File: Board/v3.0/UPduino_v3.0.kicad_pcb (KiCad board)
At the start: 4 copper layers, 62 x 22.2 mm, 114 parts, among them J1 47589-0001, J2 Right, J3 Left, J4 5V Power, U1 93LC56BT-I/OT, U2 ICE40UP5K-SG48ITR, U3 FT232H, U4 SG-210STF 12.0000ML3, U5 W25Q32JVSSIM, U6 AP2127K-3.3, U7 AP2127K-1.2, U8 SN74AUP2G125DCUR

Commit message: Removed CE logo, added RoHS logo, regenerated gerbers.
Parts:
- removed the REF** at (125.6, 92.5)
- added REF**: RoHS-Logo_3mm_SilkScreen, Symbol:RoHS-Logo_3mm_SilkScreen - Copy, B.Cu at (134.3, 94.9)

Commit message: Updated gerbers and fab files
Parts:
- moved D3 0.25 mm to (110.9, 87.0)
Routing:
- net /LED_B: track 42.5 -> 44.2 mm
- net /IOT_51A: track 15.4 -> 14.5 mm

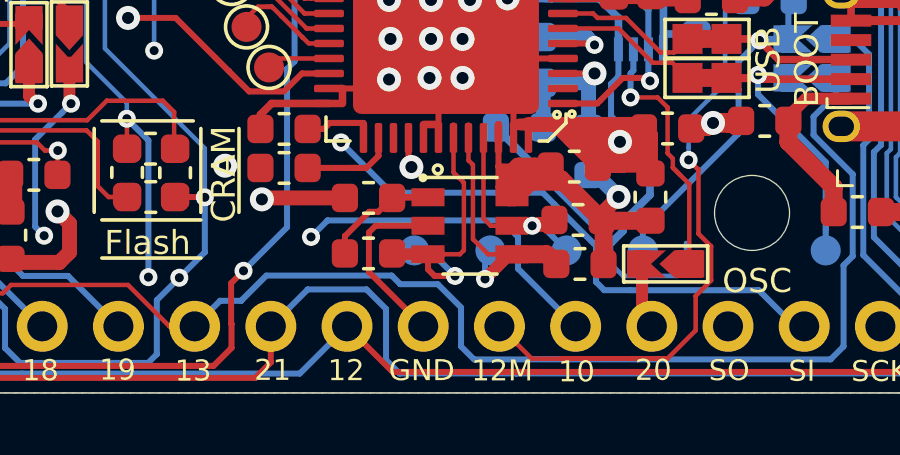
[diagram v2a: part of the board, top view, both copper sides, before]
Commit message: Bugfix for 12MHz clock pin
@ggrummer identified a bug that the 12MHz clock and ground pins are swapped.
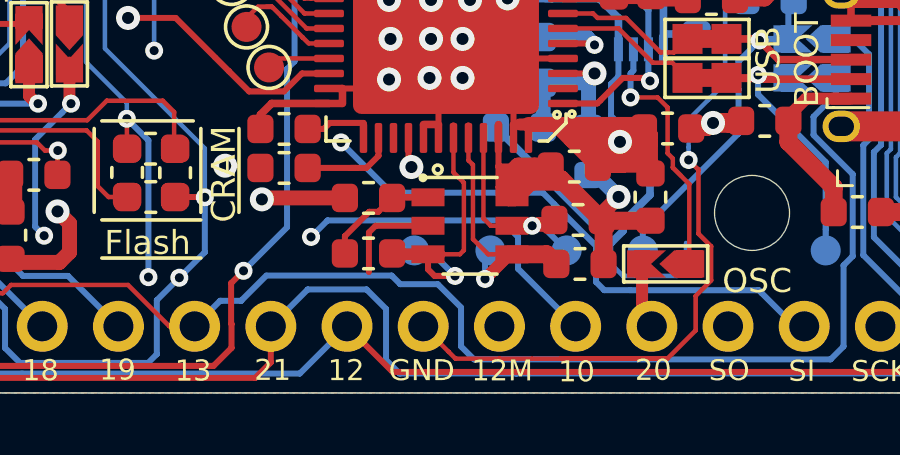
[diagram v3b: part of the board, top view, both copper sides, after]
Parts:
- removed the REF** at (134.3, 94.9)
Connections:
- J3 pad 7: /CLK_12M_EXT -> GND
- J3 pad 8: GND -> /CLK_12M_EXT
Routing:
- net GND: track 283.3 -> 280.7 mm
- net /CLK_12M_EXT: track 38.2 -> 40.7 mm

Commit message: Added country of origin USA on back silkscreen
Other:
- board text added: "Made in The USA"
